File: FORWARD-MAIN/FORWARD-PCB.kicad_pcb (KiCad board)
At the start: 2 copper layers, 96.3 x 67.5 mm, 46 parts, among them J1 USB_B_Micro, J2 Conn_01x03_Socket, J5 Conn_01x14_Pin, Q1 SS8050-G, Q2 SS8050-G, U1 BNO055, U2 CP2102N, U5 ESP32-WROOM-32D

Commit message: minor tweaks
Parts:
- U2: value CP2102N -> CP2102N-Axx-xQFN28
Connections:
- U1 pad 15: unconnected-(U1-GNDIO-Pad15) -> unconnected-(U1-GNDIO-Pad15)_1
- U1 pad 16: unconnected-(U1-GNDIO-Pad15) -> unconnected-(U1-GNDIO-Pad15)_2
- U5 pad 39: unconnected-(U5-IO39-Pad39) -> /ECHO_2
- U5 pad 4: /TRIG_2 -> unconnected-(U5-SENSOR_VP-Pad4)
- U5 pad 5: /ECHO_2 -> unconnected-(U5-SENSOR_VN-Pad5)
- U5 pad 9: unconnected-(U5-IO33-Pad9) -> /TRIG_2

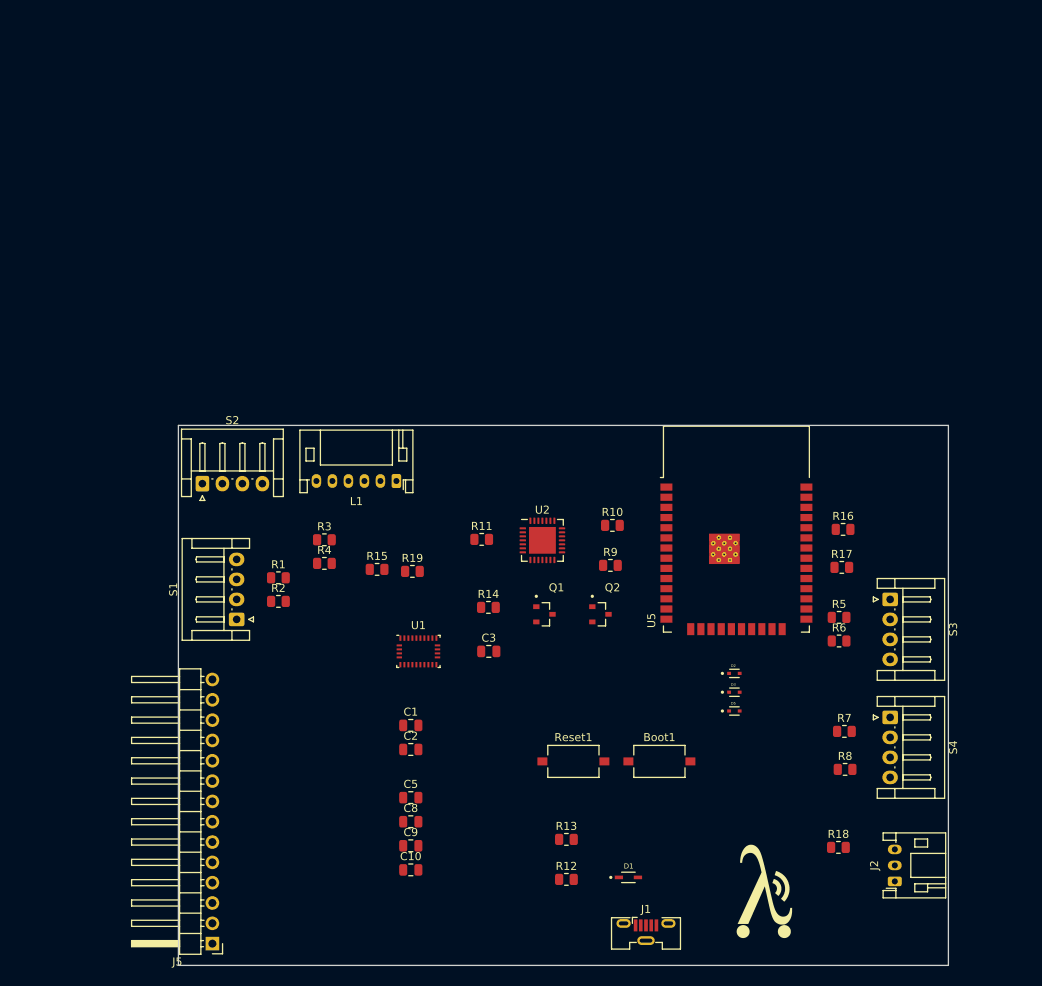
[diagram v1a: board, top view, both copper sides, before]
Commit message: autorouting trying but failing
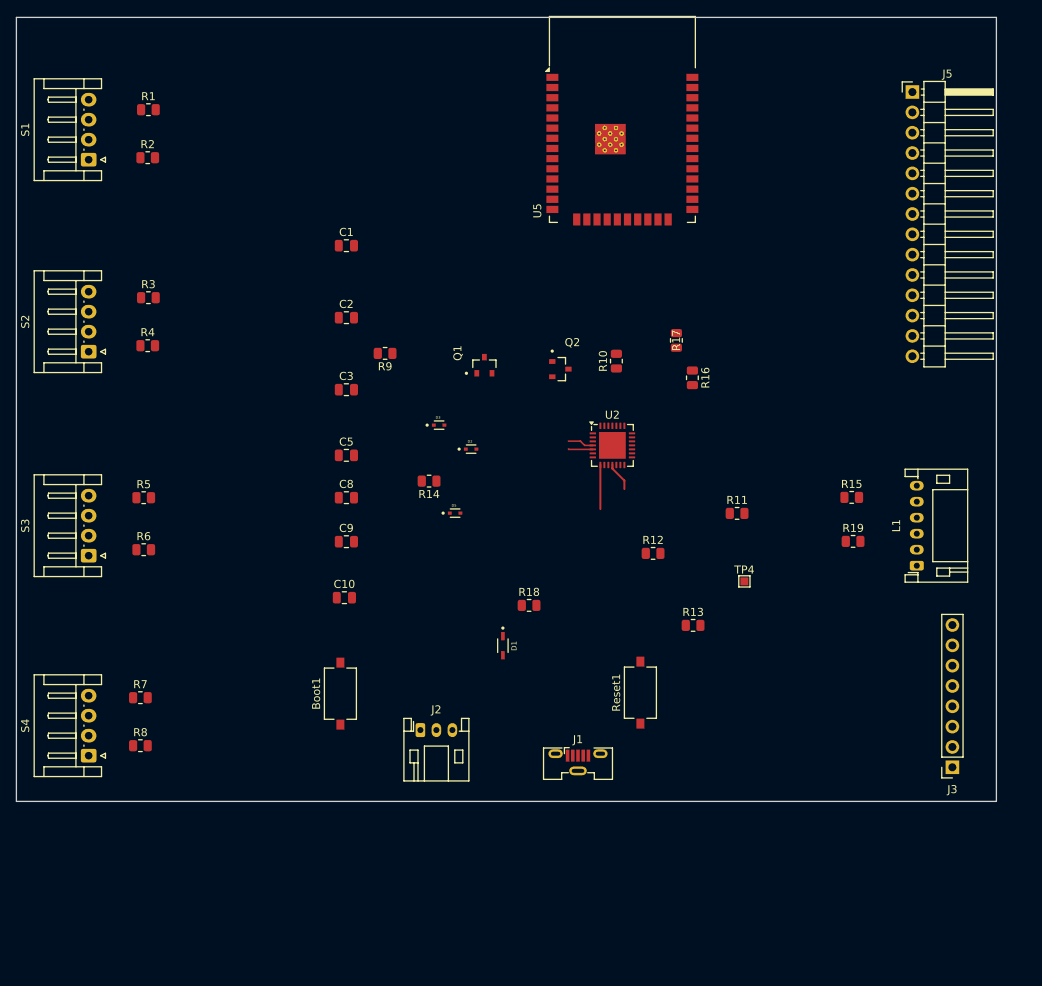
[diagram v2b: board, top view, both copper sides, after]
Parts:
- removed G***: LOGO, PCB design:lambda
- removed U1: BNO055, Package_LGA:LGA-28_5.2x3.8mm_P0.5mm
- added J3: Conn_01x08_Socket, Connector_PinSocket_2.54mm:PinSocket_1x08_P2.54mm_Vertical, F.Cu at (187.3, 139.5)
- added TP4: TestPoint, TestPoint:TestPoint_Pad_1.0x1.0mm, F.Cu at (161.3, 116.3)
- D1: footprint pcb-footprints:SOD2513X120N -> footprints:SOD2513X120N
- D2, D3, D5: footprint pcb-footprints:TVS_LESD5D5.0CT1G -> footprints:TVS_LESD5D5.0CT1G
- Q1, Q2: footprint pcb-footprints:TRANS_SS8050-G -> footprints:TRANS_SS8050-G
- moved J5 137.8 mm to (182.3, 55.1), turned to 0 degrees
- moved S3 100.3 mm to (79.3, 113.1), turned to 90 degrees
- moved S4 100.3 mm to (79.3, 138.1), turned to 90 degrees
- moved R5 88.2 mm to (86.2, 105.8)
- moved R8 88.1 mm to (85.8, 136.8)
- moved R7 88.1 mm to (85.8, 130.8)
- moved R6 87.7 mm to (86.2, 112.3)
- moved L1 65.9 mm to (182.8, 114.3), turned to 90 degrees
- moved J2 62.2 mm to (120.8, 134.9), turned to 0 degrees
- moved R1 60.7 mm to (86.8, 57.3)
- moved C1 60.5 mm to (111.5, 74.3)
- moved S1 60.4 mm to (79.3, 63.6)
- moved R15 60.0 mm to (174.7, 105.8)
- moved R2 57.8 mm to (86.7, 63.3)
- moved R19 55.2 mm to (174.9, 111.3)
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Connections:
- Boot1 pad 2: /EN -> /IO0
- Reset1 pad 2: /IO0 -> /EN
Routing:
- net Net-(U2-VBUS): track 0.00 -> 5.52 mm
- net /ACTIVE: track 0.00 -> 3.64 mm
- net /USB_DP: track 0.00 -> 3.27 mm
- net /USB_DN: track 0.00 -> 3.06 mm
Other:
- board size 96.3 x 67.5 mm -> 122.5 x 98 mm
- copper layers 2 -> 4

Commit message: routing progress
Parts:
- J5: value Conn_01x14_Pin -> Conn_01x14_Socket; footprint Connector_PinHeader_2.54mm:PinHeader_1x14_P2.54mm_Horizontal -> Connector_Phoenix_MC:PhoenixContact_MC_1,5_14-G-3.81_1x14_P3.81mm_Horizontal
- moved J5 44.1 mm to (188.3, 98.8), turned to 90 degrees
- moved C2 41.8 mm to (153.3, 81.8)
- moved C5 40.2 mm to (97.3, 138.1), turned to 180 degrees
- moved C10 36.6 mm to (146.8, 127.3), turned to -90 degrees
- moved C1 33.5 mm to (144.8, 78.3)
- moved C3 31.4 mm to (97.3, 120.3)
- moved C8 30.5 mm to (97.3, 132.8), turned to 180 degrees
- moved J3 28.5 mm to (164.3, 122.8), turned to 0 degrees
- moved R17 28.2 mm to (124.8, 82.8)
- moved R16 25.3 mm to (130.8, 82.8)
- moved R14 24.1 mm to (143.8, 113.8), turned to -90 degrees
- moved R9 23.2 mm to (139.3, 84.3), turned to 0 degrees
- moved C9 20.9 mm to (97.5, 126.8), turned to 180 degrees
- moved R13 20.9 mm to (137.8, 109.8), turned to -90 degrees
- moved R18 19.2 mm to (152.8, 124.8)
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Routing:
- net /TRIG_4: track 0.00 -> 103.4 mm
- net /ECHO_4: track 0.00 -> 101.3 mm, vias 0 -> 2
- net /ECHO_3: track 0.00 -> 87.9 mm, vias 0 -> 4
- net /TRIG_3: track 0.00 -> 82.5 mm
- net /TRIG_2: track 0.00 -> 73.8 mm, vias 0 -> 2
- net /ECHO_2: track 0.00 -> 73.0 mm, vias 0 -> 2
- net /EN: track 0.00 -> 70.4 mm
- net /TRIG_1: track 0.00 -> 59.7 mm, vias 0 -> 1
- net /Wheels-IO23: track 0.00 -> 35.0 mm, vias 0 -> 2
- net /P0W: track 0.00 -> 29.6 mm, vias 0 -> 2
- net /IO0: track 0.00 -> 24.9 mm
- net /VBUS: track 0.00 -> 24.8 mm
- net /USB_DP: track 3.27 -> 24.0 mm
- net /USB_DN: track 3.06 -> 23.1 mm
- net /RTS: track 0.00 -> 16.2 mm
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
